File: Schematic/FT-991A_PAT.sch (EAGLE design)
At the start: 31 parts, among them Q1 PE4259, Q2 MC78L09ABDR2GOSCT, Q5 NCP553, Q7 J310, Q8 BFR193F, X1 IF_IN, X2 SCP_OUT, X3 SDR_OUT

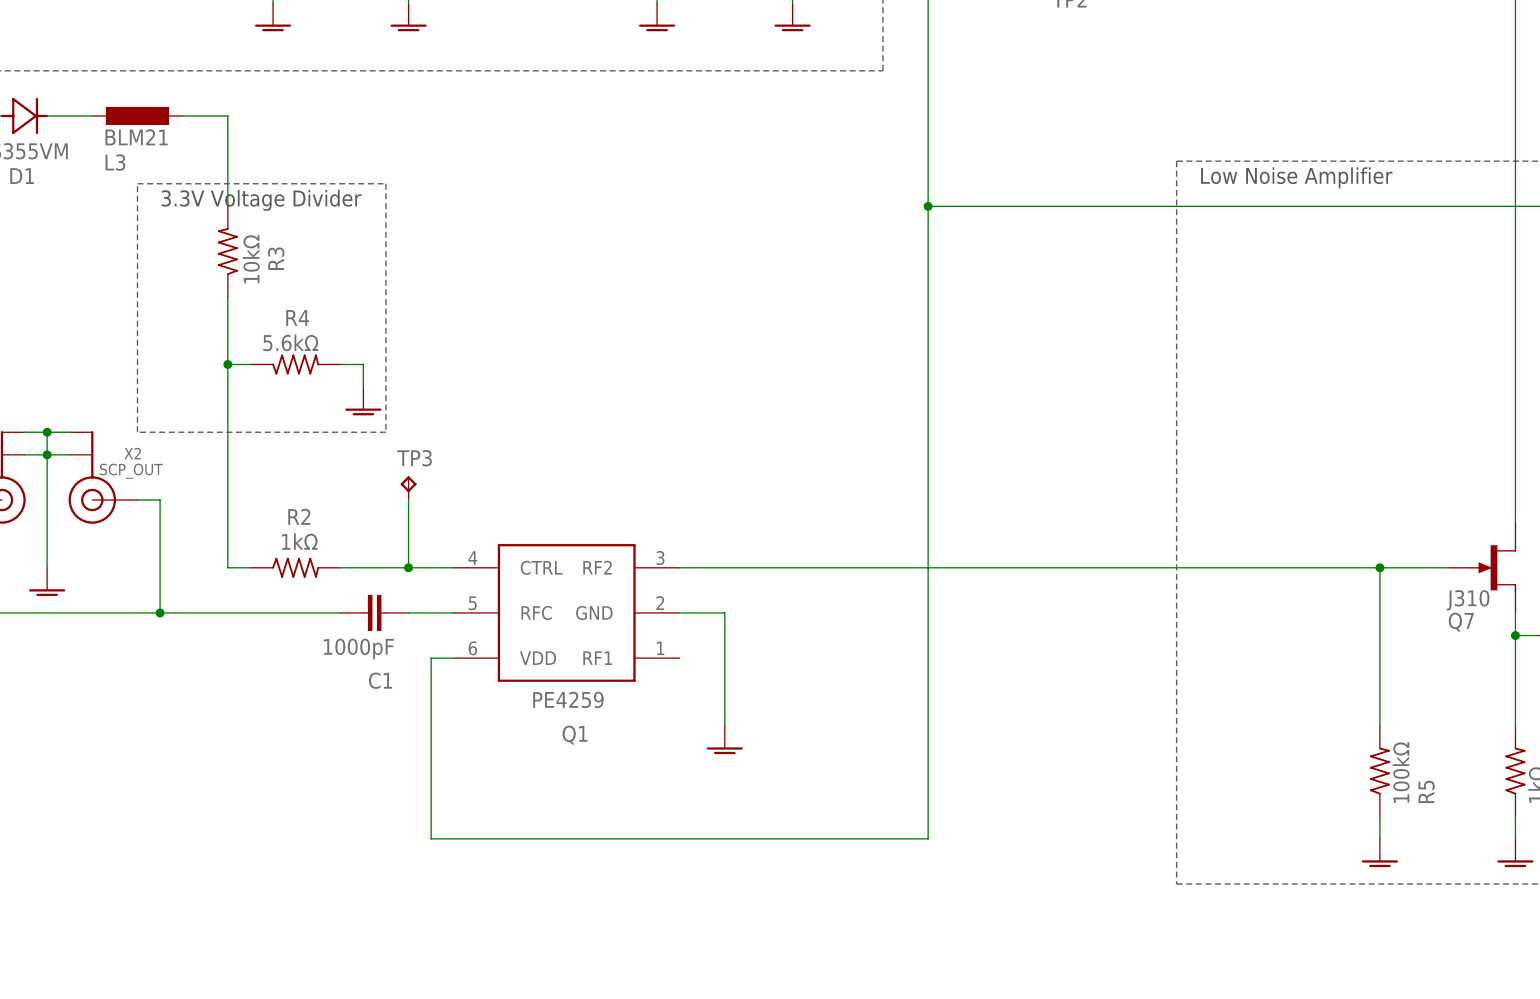
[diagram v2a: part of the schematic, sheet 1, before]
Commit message: Rev. S: New RF switch actuation
* New RF switch design - now uses an analog switch to flip the RF switch.
  While this added new parts (1 switch and two resistors) and extra
  complexity, this actuation format is industry-standard and allows
  for substitutes of PE4259 (which is unobtanium as of now).

* New component in library (NLAS4599)
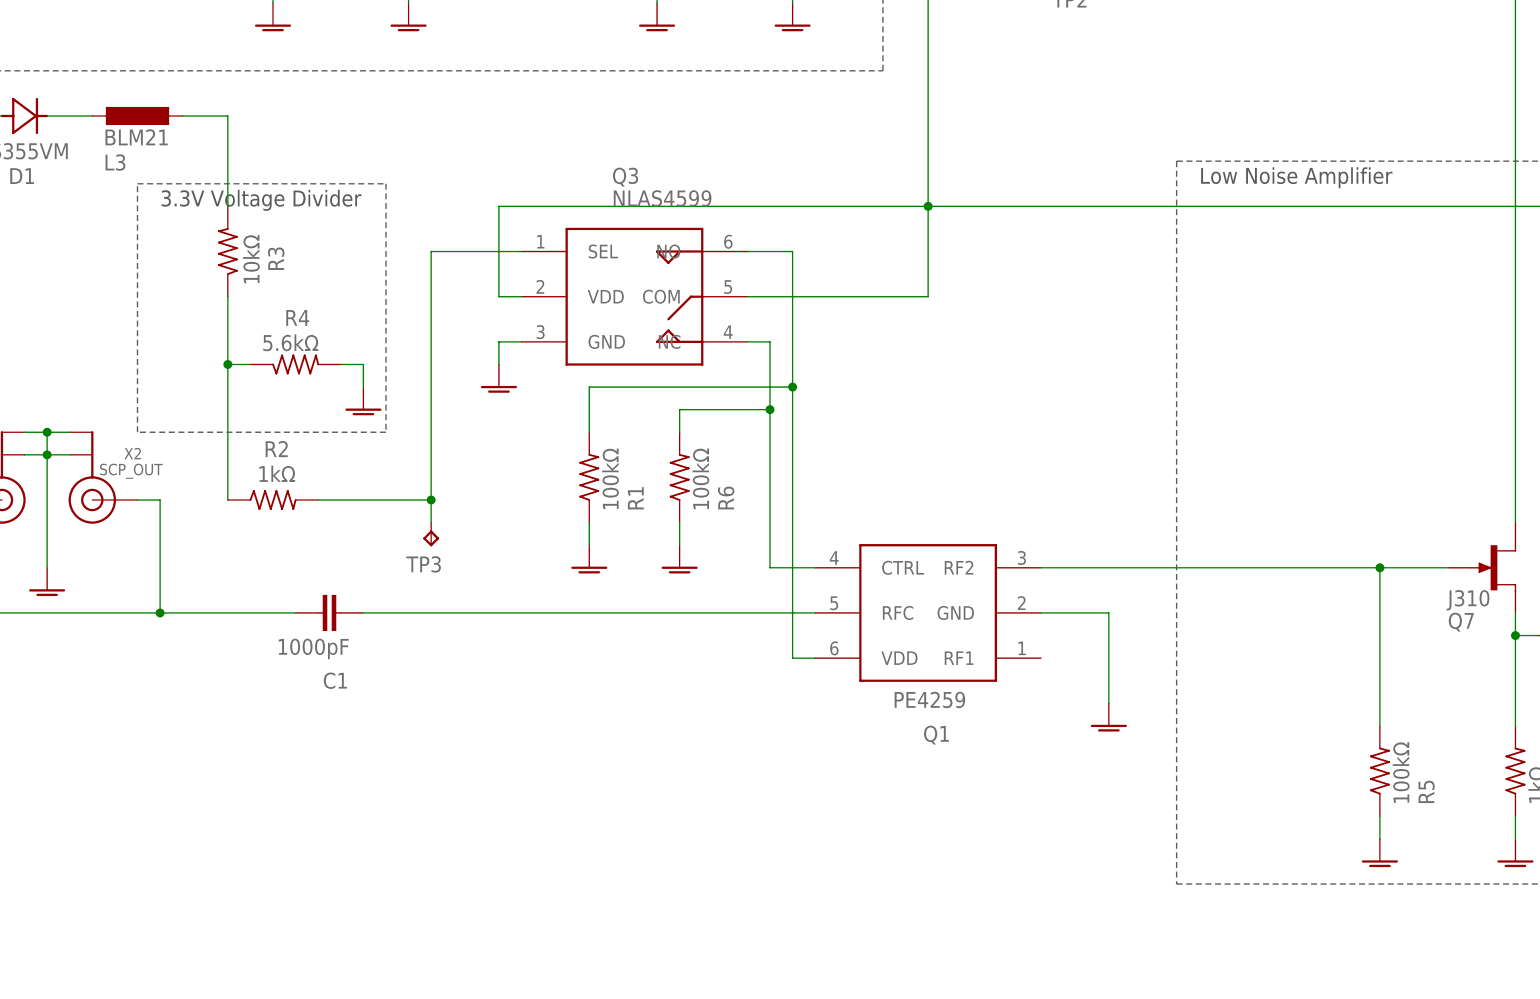
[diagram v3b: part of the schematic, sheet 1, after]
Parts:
- added Q3: NLAS4599, aarf:NLAS4599
- added R1, R6: 100kΩ, aarf:R-1206
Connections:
- new net N$2: Q1.CTRL, Q3.NC, R6.2
- new net N$6: Q1.VDD, Q3.NO, R1.2
- net 3V: now also Q3.COM, Q3.VDD; no longer Q1.VDD
- net GNDA: now also Q3.GND, R1.1, R6.1
- net N$7: now also Q3.SEL; no longer Q1.CTRL
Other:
- moved on the sheet: C1, Q1, R2, TP3

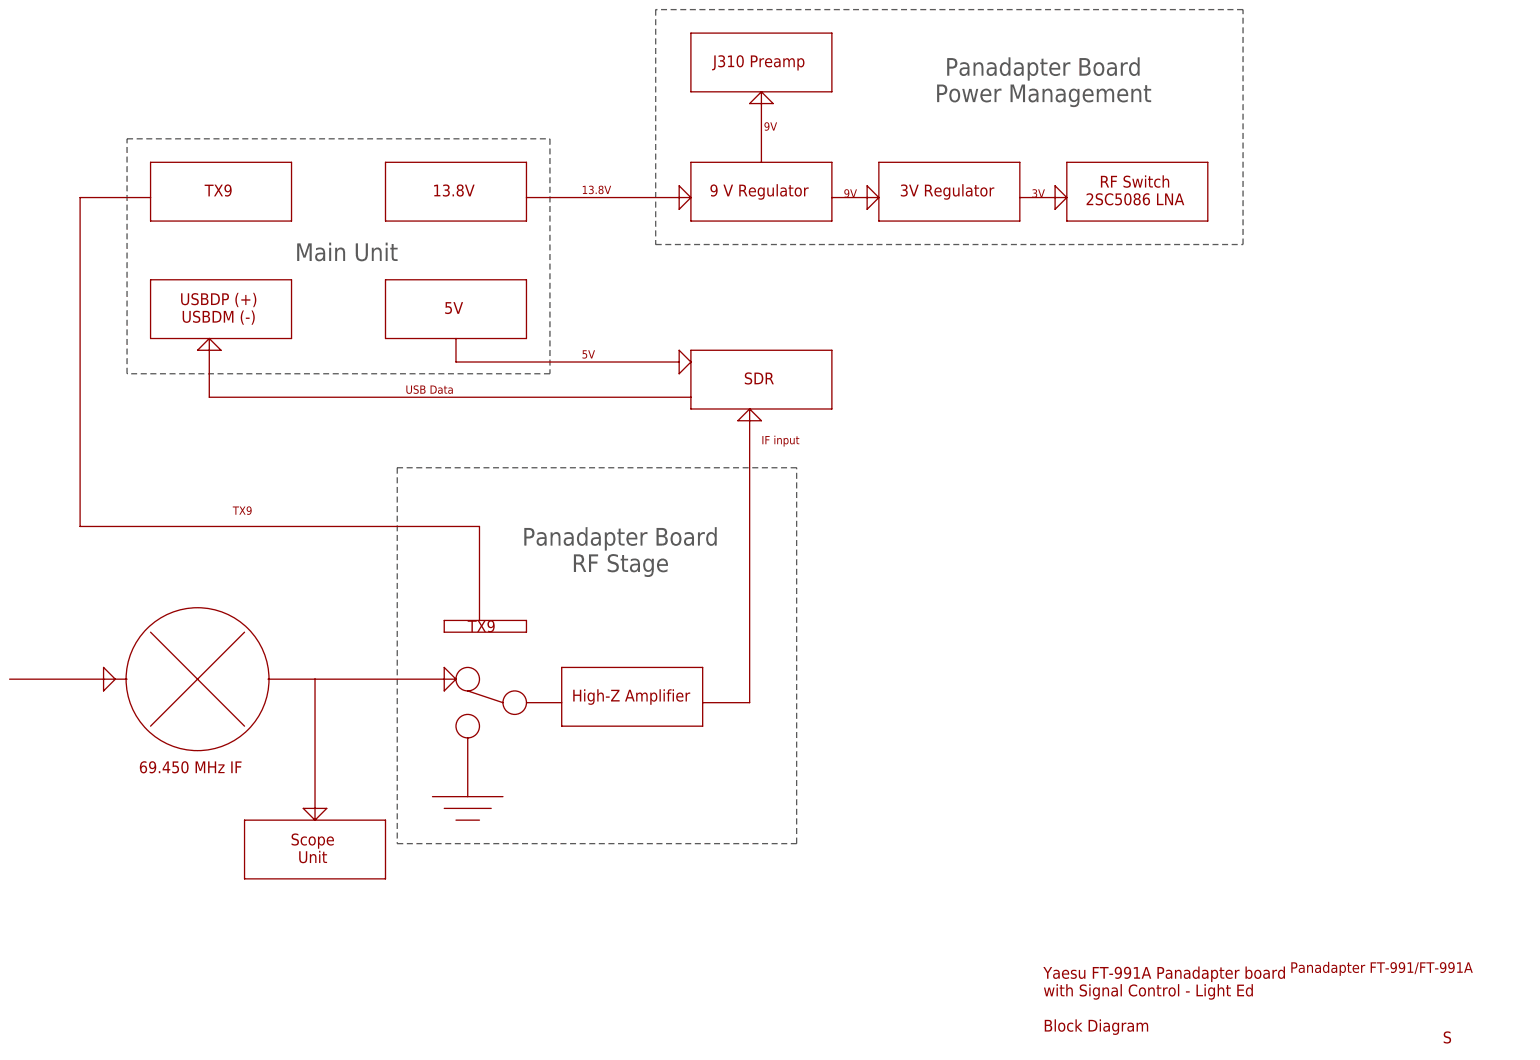
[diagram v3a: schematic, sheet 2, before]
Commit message: Revision S improvements
- Very minor changes on board design around the power regulator,
  allowing for extra clearance for part description
- Replaced the EOLed OnSemi switch with an active Vishay one
- Updated the overall board block diagram
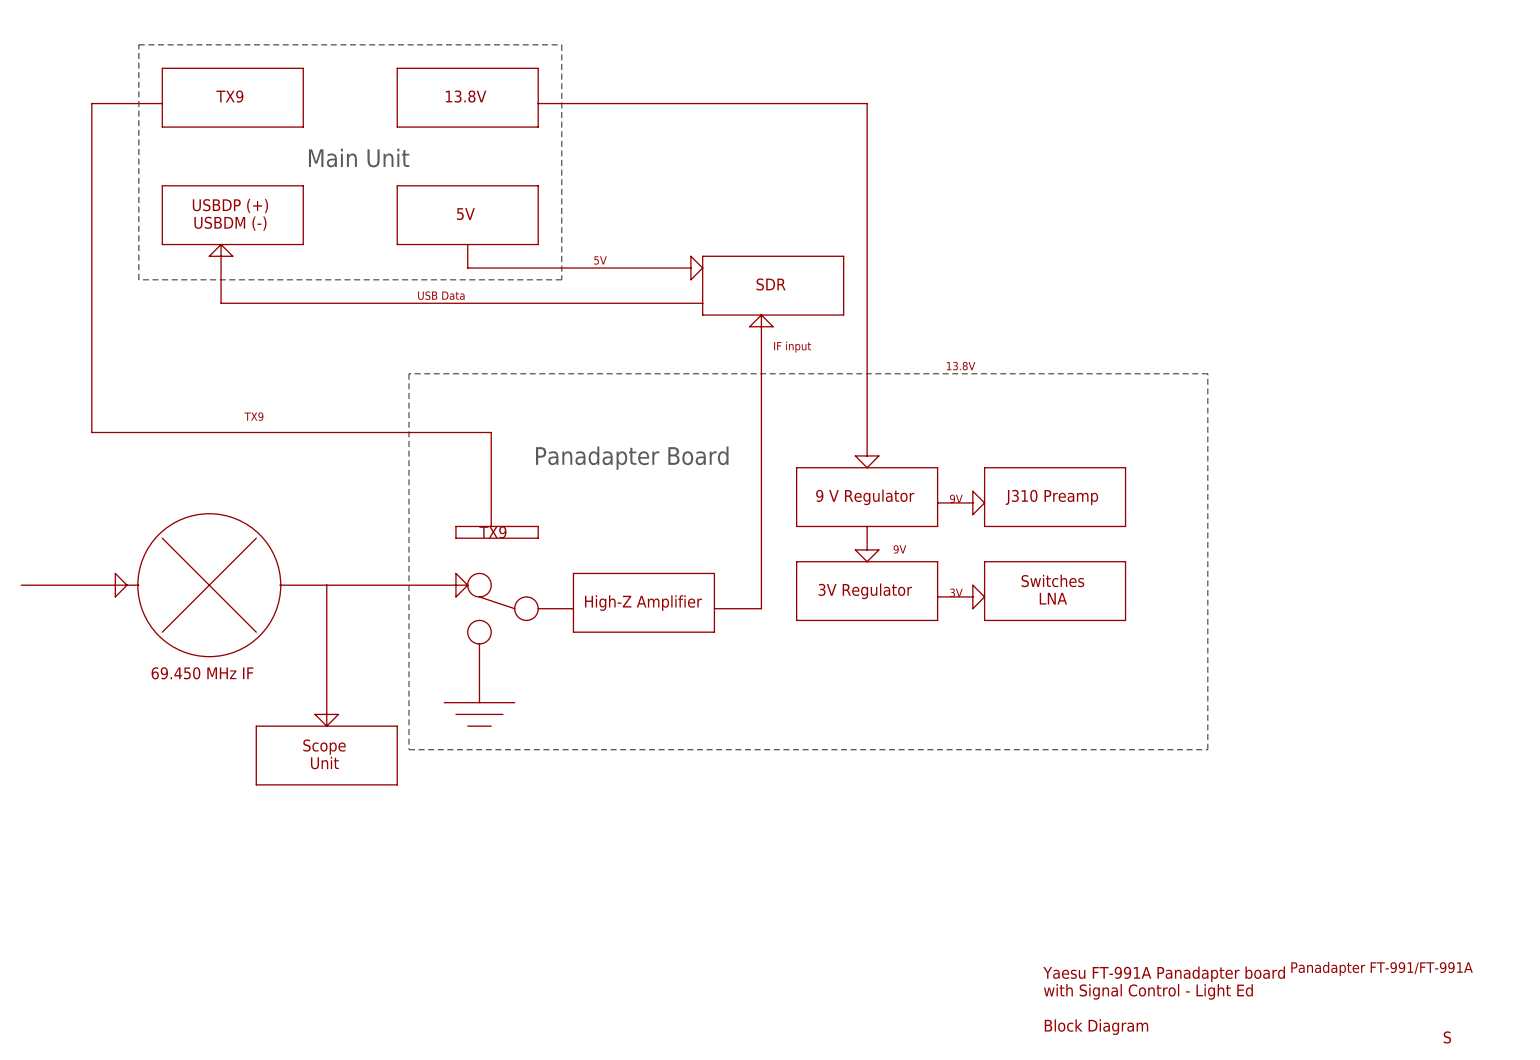
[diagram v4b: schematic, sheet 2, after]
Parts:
- Q2: value MC78L09ABDR2GOSCT -> MC78L09
- Q3: value NLAS4599 -> DG2001
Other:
- note added: "Panadapter Board"
- note added: "Switches LNA"
- note removed: "Panadapter Board Power Management"
- note removed: "Panadapter Board RF Stage"
- note removed: "RF Switch 2SC5086 LNA"

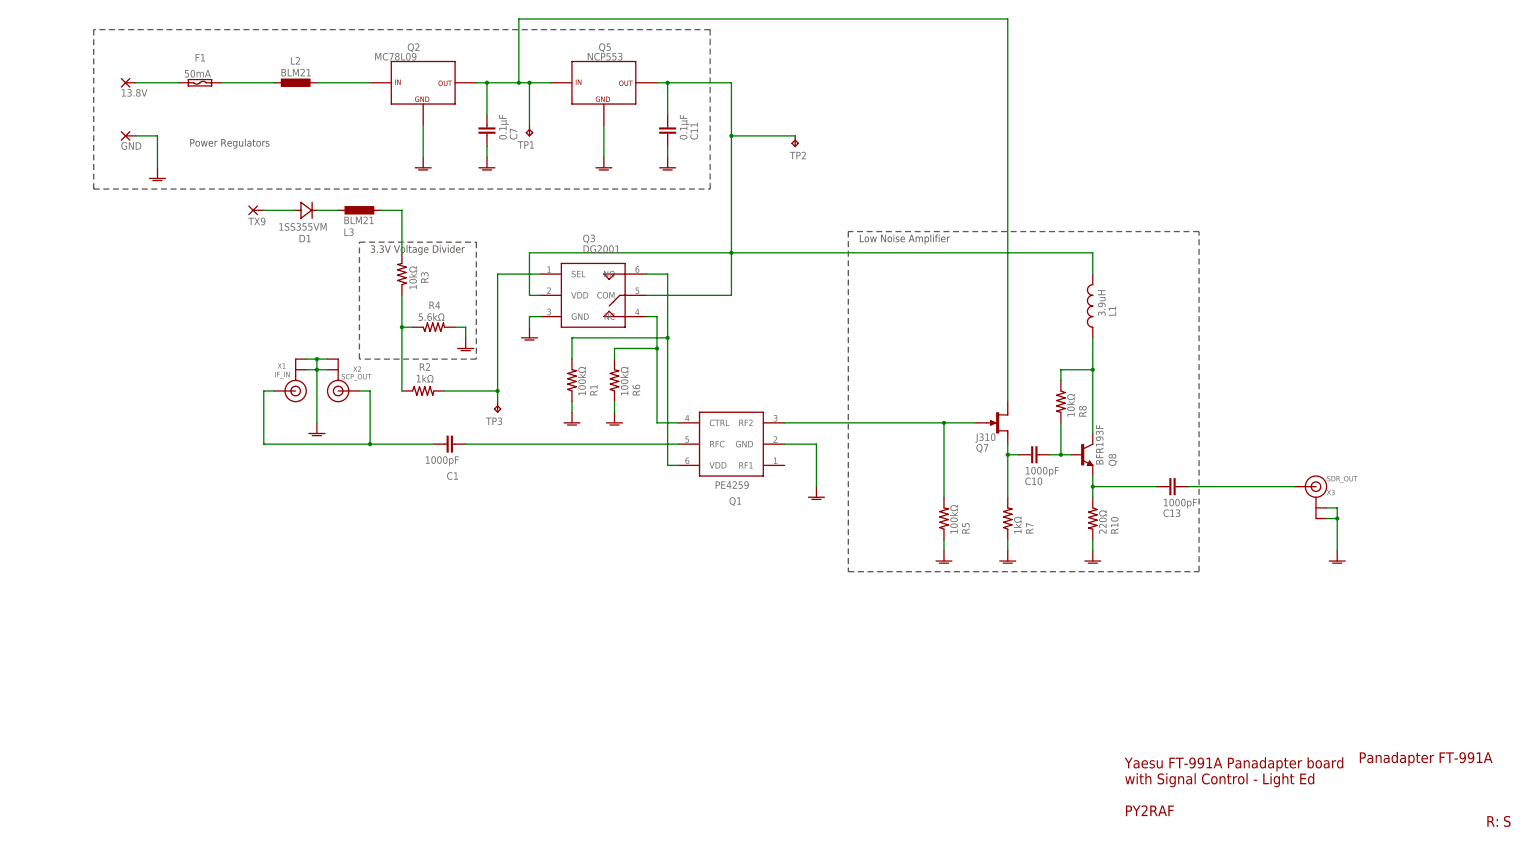
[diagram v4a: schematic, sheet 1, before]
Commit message: Featuring: Revision T
* Fixed a gross flaw in Revision S: The RF switch was flipped out /o\  Resolves #25
* Updated BOM, renamed some capacitors and the matching network components are labeled as {C,R}1x
* There are more gain to be obtained from BFR193. Added a bias and matching network design from [Infineon's AN-1806](https://www.infineon.com/dgdl/Infineon-Design_Guide_for_low_noise_TR_in_FM_radio_FE-ApplicationNotes-v01_00-EN.pdf?fileId=8ac78c8c7e7124d1017f0227976a6c9d). While the matching network isn't suitable for BFR193, the footprints will be good enough to test other components and values. Capacitors are 0805, Resistors are 1206.
* This revision is planned to be a testbed for a proper bias and match network in order to get better gain figures from BFR193.

Signed-off-by: Rodrigo Freire <py2raf@rf3.org>
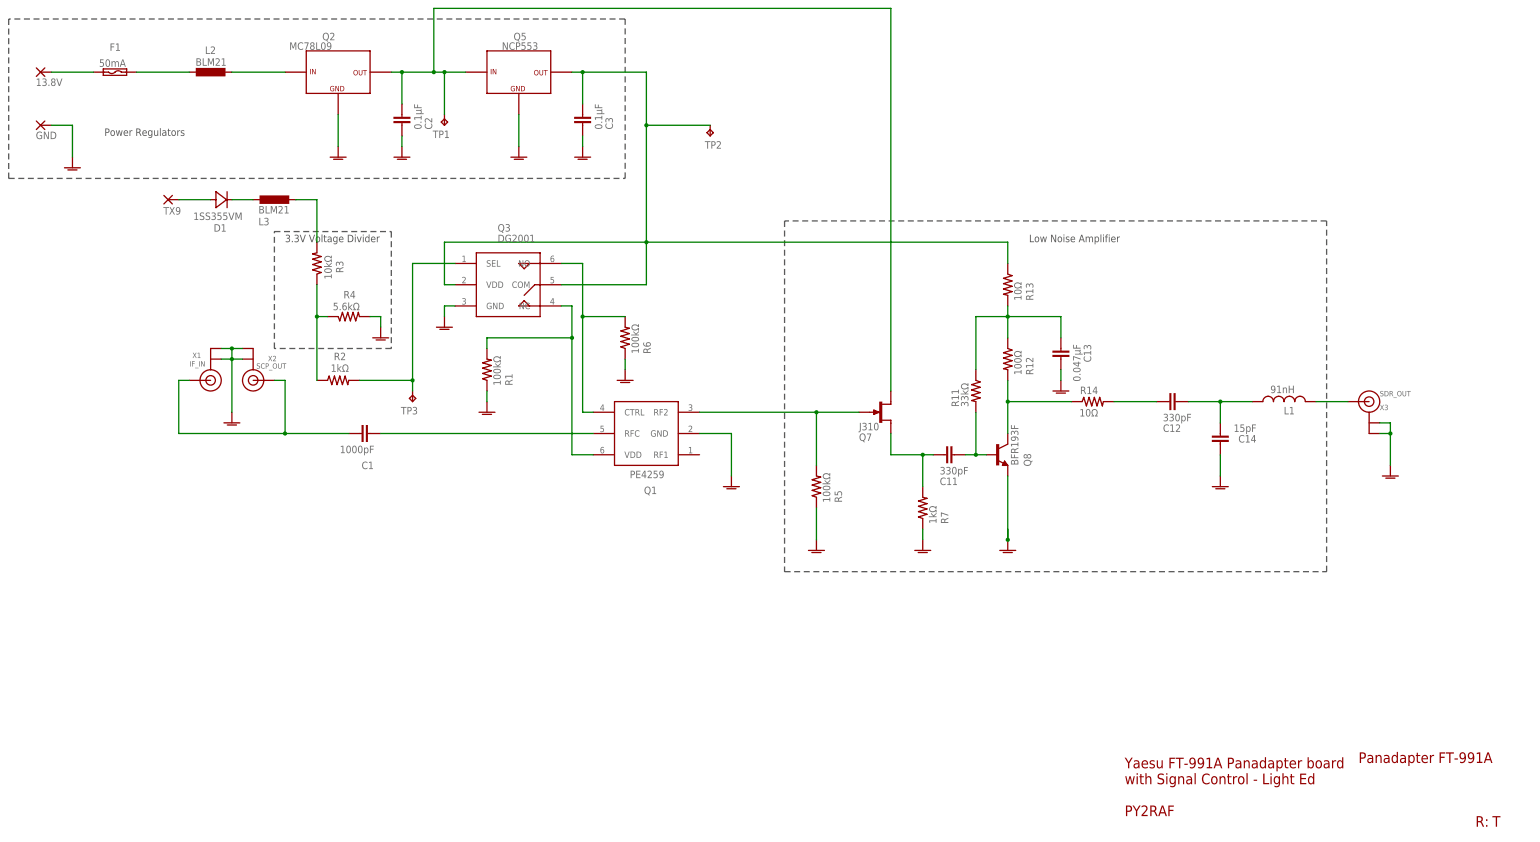
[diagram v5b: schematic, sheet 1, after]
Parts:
- removed C10: 1000pF, aarf:C-0805
- removed C7: 0.1µF, aarf:C-1206
- removed R10: 220Ω, aarf:R-1206
- removed R8: 10kΩ, aarf:R-1206
- added C12: 330pF, aarf:C-0805
- added C14: 15pF, aarf:C-0805
- added C2, C3: 0.1µF, aarf:C-1206
- added R11: 33kΩ, aarf:R-1206
- added R12: 100Ω, aarf:R-1206
- added R13, R14: 10Ω, aarf:R-1206
- C11: value 0.1µF -> 330pF; device aarf:C-1206 -> aarf:C-0805
- C13: value 1000pF -> 0.047µF
- L1: value 3.9uH -> 91nH; MODEL (none) -> LQW2BAN91NJ00L; SPICEPREFIX (none) -> L
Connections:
- removed net N$2: Q1.CTRL, Q3.NC, R6.2
- removed net N$6: Q1.VDD, Q3.NO, R1.2
- new net BIAS: Q8.C, R12.2, R14.1
- new net N$3: C12.1, R14.2
- new net NC: Q1.VDD, Q3.NC, R1.2
- new net NO: Q1.CTRL, Q3.NO, R6.2
- net 3V: now also C3.1, R13.1; no longer C11.1, L1.1
- net 9V: now also C2.1; no longer C7.1
- net FB-3V: now also C13.1, R11.1, R12.1, R13.2; no longer L1.2, Q8.C, R8.1
- net FINAL: now also L1.2; no longer C13.2
- net GNDA: now also C13.2, C14.1, C2.2, C3.2, Q8.E; no longer C11.2, C7.2, R10.2
- net N$1: now also C12.2, C14.2, L1.1; no longer C13.1, Q8.E, R10.1
- net N$4: now also C11.2, R11.2; no longer C10.2, R8.2
- net N$5: now also C11.1; no longer C10.1
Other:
- moved on the sheet: C1, C11, C13, D1, F1, L1, L2, L3, Q1, Q2, Q3, Q5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
